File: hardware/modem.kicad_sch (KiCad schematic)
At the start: 30 parts, among them J11 PRPC001DAAN-RC, Q3 IRLML2246TRPBF, Q4 MMBT3904, U6 SN74AVC4T245PW, U7 SARA-R500S-61B

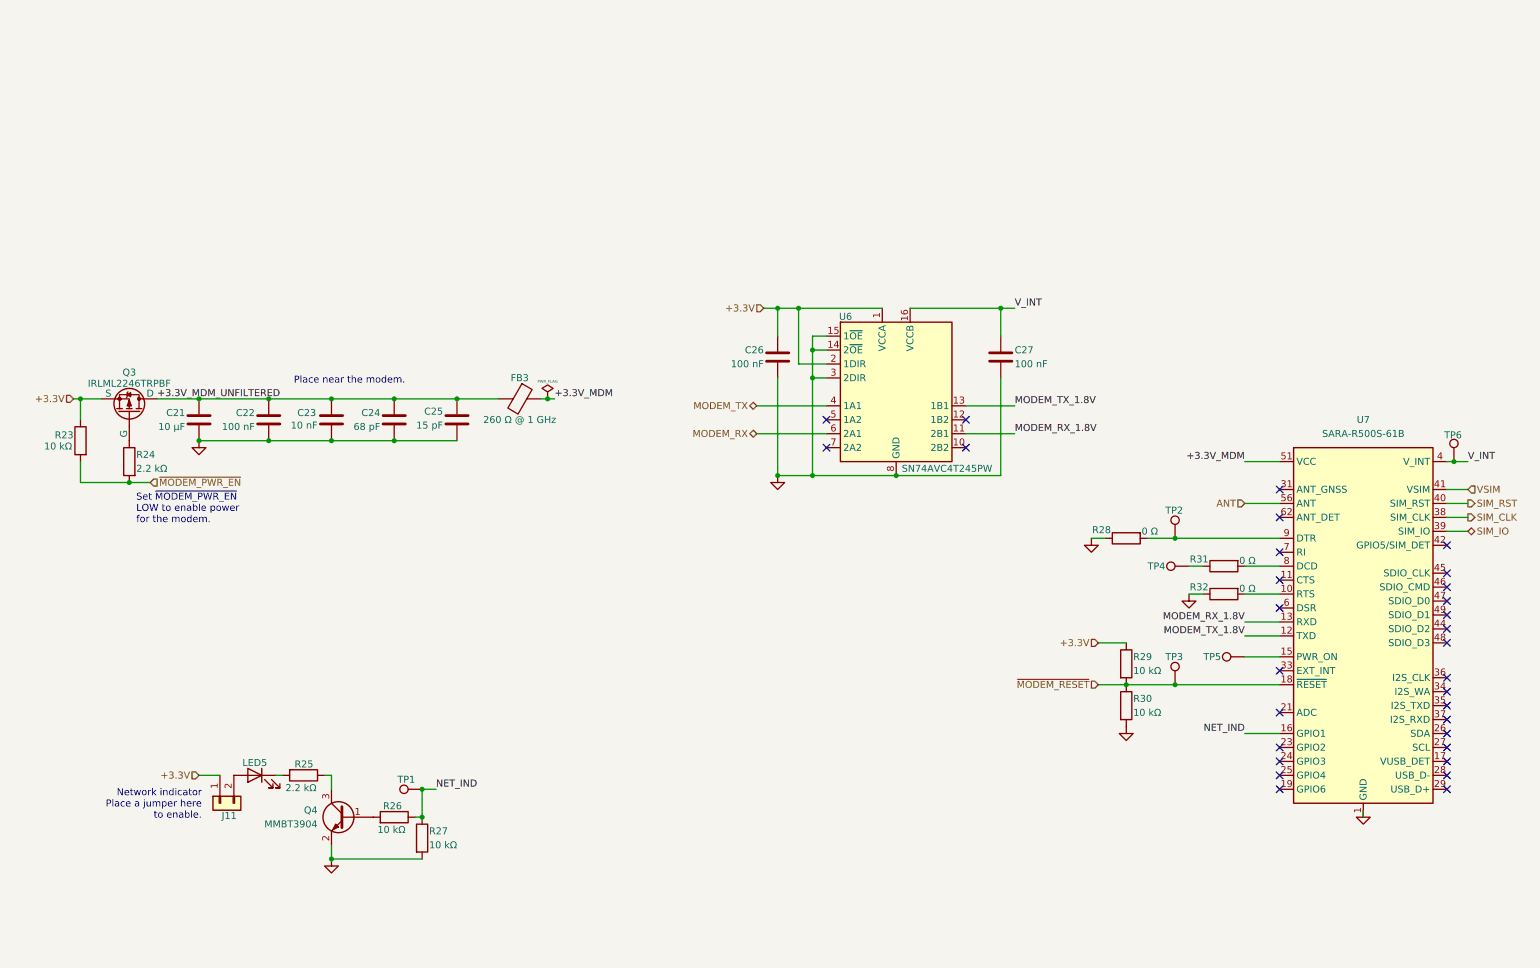
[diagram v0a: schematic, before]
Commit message: HW: Start adding Li-Po support
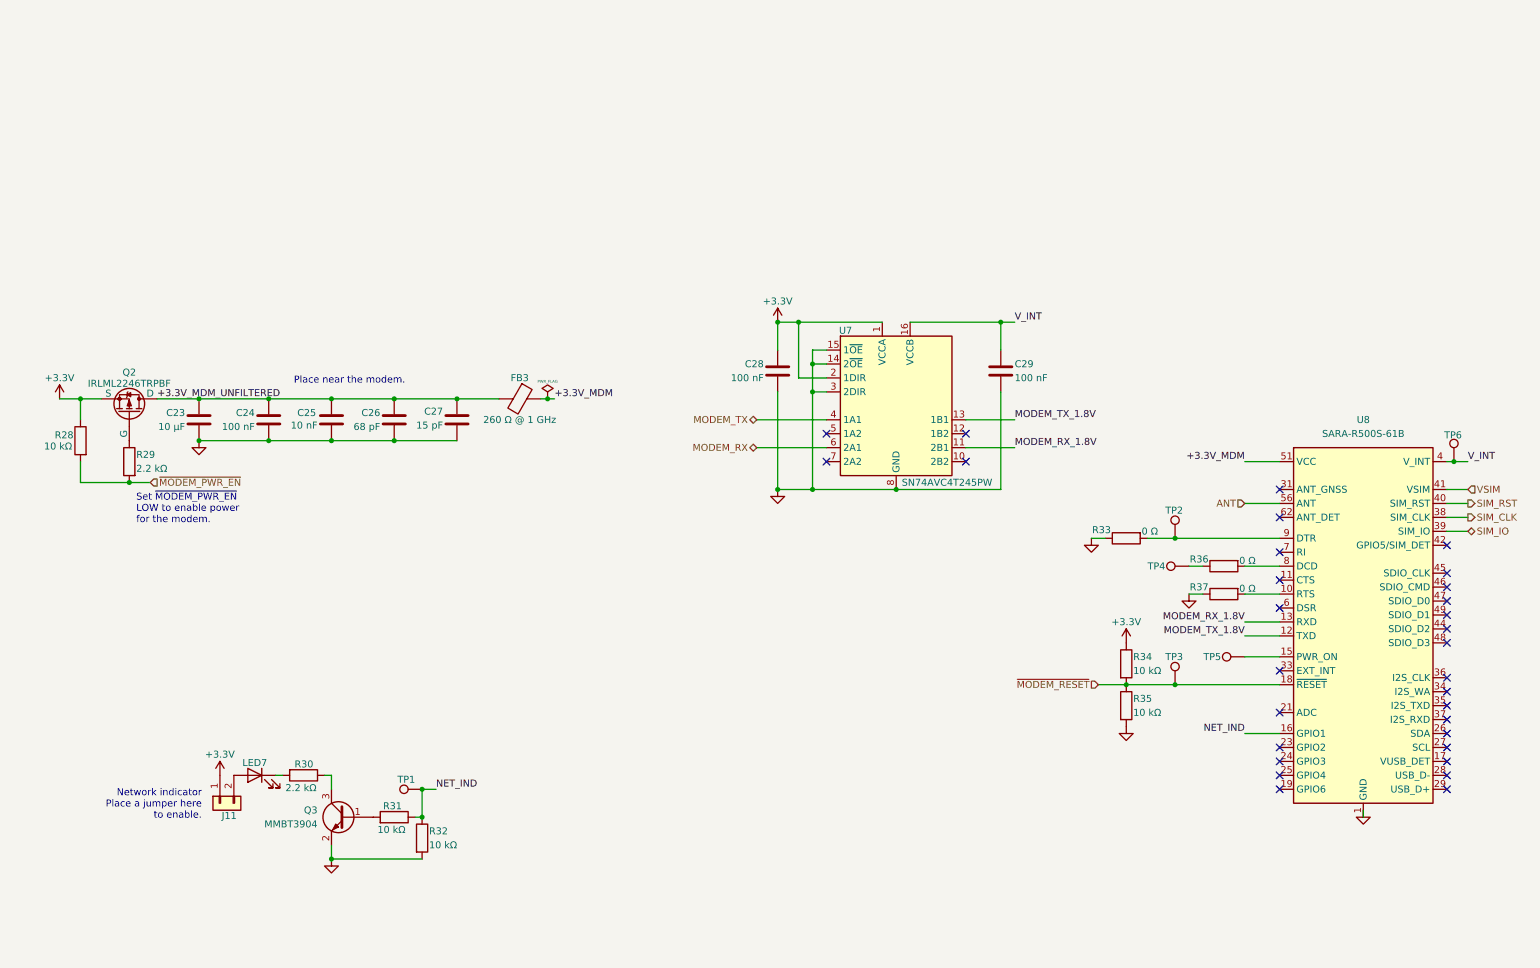
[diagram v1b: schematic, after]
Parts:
- renumbered C21 to C23, C22 to C24, C23 to C25, C24 to C26, C25 to C27, C26 to C28, C27 to C29, LED5 to LED7, Q3 to Q2, Q4 to Q3, R23 to R28, R24 to R29, R25 to R30, R26 to R31, R27 to R32, R28 to R33, R29 to R34, R30 to R35, R31 to R36, R32 to R37, U6 to U7, U7 to U8
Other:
- moved on the sheet: C28, C29, U7

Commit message: HW: Replace STM QFN with QFP
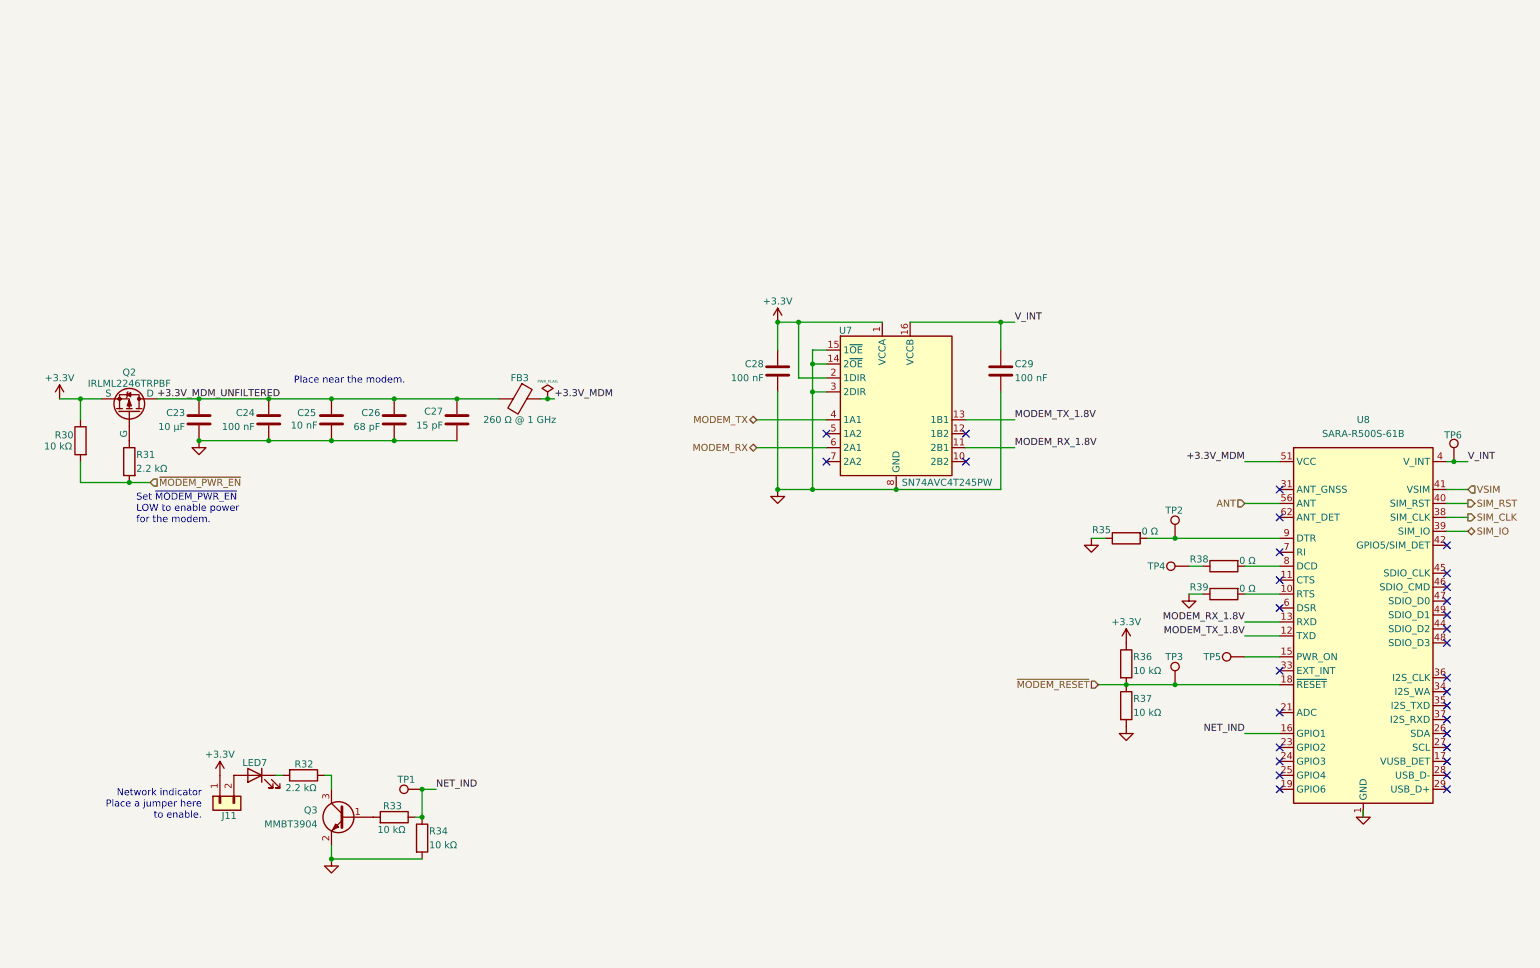
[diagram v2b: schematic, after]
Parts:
- renumbered R28 to R30, R29 to R31, R30 to R32, R31 to R33, R32 to R34, R33 to R35, R34 to R36, R35 to R37, R36 to R38, R37 to R39
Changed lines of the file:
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@@
 		(on_board yes)
 		(dnp no)
-		(property "Reference" "R34"
+		(property "Reference" "R36"
 			(at 213.36 134.62 0)
 			(effects
@@
 			(project "iida_devkit"
 				(path "/b12a6e25-97fb-4aba-bc96-af8db389bb9a/3723475b-e956-4027-ac40-e47346743900"
-					(reference "R34")
+					(reference "R36")
 					(unit 1)
 				)
@@
 		(on_board yes)
 		(dnp no)
-		(property "Reference" "#PWR040"
+		(property "Reference" "#PWR043"
 			(at 46.99 160.02 0)
 			(effects
@@
 			(project "iida_devkit"
 				(path "/b12a6e25-97fb-4aba-bc96-af8db389bb9a/3723475b-e956-4027-ac40-e47346743900"
-					(reference "#PWR040")
+					(reference "#PWR043")
 					(unit 1)
 				)
@@
 		(on_board yes)
 		(dnp no)
-		(property "Reference" "R31"
+		(property "Reference" "R33"
 			(at 76.708 161.798 90)
 			(effects
@@
 			(project "iida_devkit"
 				(path "/b12a6e25-97fb-4aba-bc96-af8db389bb9a/3723475b-e956-4027-ac40-e47346743900"
-					(reference "R31")
+					(reference "R33")
 					(unit 1)
 				)
@@
 		(on_board yes)
 		(dnp no)
-		(property "Reference" "R35"
+		(property "Reference" "R37"
 			(at 213.36 142.24 0)
 			(effects
@@
 			(project "iida_devkit"
 				(path "/b12a6e25-97fb-4aba-bc96-af8db389bb9a/3723475b-e956-4027-ac40-e47346743900"
-					(reference "R35")
+					(reference "R37")
 					(unit 1)
 				)
@@
 		(on_board yes)
 		(dnp no)
-		(property "Reference" "#PWR045"
+		(property "Reference" "#PWR048"
 			(at 212.09 135.89 0)
 			(effects
@@
 			(project "iida_devkit"
 				(path "/b12a6e25-97fb-4aba-bc96-af8db389bb9a/3723475b-e956-4027-ac40-e47346743900"
-					(reference "#PWR045")
+					(reference "#PWR048")
 					(unit 1)
 				)
@@
 		(on_board yes)
 		(dnp no)
-		(property "Reference" "R32"
+		(property "Reference" "R34"
 			(at 85.09 166.37 0)
 			(effects
@@
 			(project "iida_devkit"
 				(path "/b12a6e25-97fb-4aba-bc96-af8db389bb9a/3723475b-e956-4027-ac40-e47346743900"
-					(reference "R32")
+					(reference "R34")
 					(unit 1)
 				)
@@
 		(on_board yes)
 		(dnp no)
-		(property "Reference" "R28"
+		(property "Reference" "R30"
 			(at 20.32 94.234 0)
 			(effects
@@
 			(project "iida_devkit"
 				(path "/b12a6e25-97fb-4aba-bc96-af8db389bb9a/3723475b-e956-4027-ac40-e47346743900"
-					(reference "R28")
+					(reference "R30")
 					(unit 1)
 				)
@@
 		(dnp no)
 		(fields_autoplaced yes)
-		(property "Reference" "#PWR046"
+		(property "Reference" "#PWR049"
 			(at 212.09 153.67 0)
 			(effects
@@
 			(project "iida_devkit"
 				(path "/b12a6e25-97fb-4aba-bc96-af8db389bb9a/3723475b-e956-4027-ac40-e47346743900"
-					(reference "#PWR046")
+					(reference "#PWR049")
 					(unit 1)
 				)
@@
 		(dnp no)
 		(fields_autoplaced yes)
-		(property "Reference" "#PWR044"
+		(property "Reference" "#PWR047"
 			(at 205.74 119.38 0)
 			(effects
@@
 			(project "iida_devkit"
 				(path "/b12a6e25-97fb-4aba-bc96-af8db389bb9a/3723475b-e956-4027-ac40-e47346743900"
-					(reference "#PWR044")
+					(reference "#PWR047")
 					(unit 1)
 				)
@@
 		(dnp no)
 		(fields_autoplaced yes)
-		(property "Reference" "#PWR048"
+		(property "Reference" "#PWR051"
 			(at 255.27 168.91 0)
 			(effects
@@
 			(project "iida_devkit"
 				(path "/b12a6e25-97fb-4aba-bc96-af8db389bb9a/3723475b-e956-4027-ac40-e47346743900"
-					(reference "#PWR048")
+					(reference "#PWR051")
 					(unit 1)
 				)
@@
 		(on_board yes)
 		(dnp no)
-		(property "Reference" "R29"
+		(property "Reference" "R31"
 			(at 31.75 97.79 0)
 			(effects
@@
 			(project "iida_devkit"
 				(path "/b12a6e25-97fb-4aba-bc96-af8db389bb9a/3723475b-e956-4027-ac40-e47346743900"
-					(reference "R29")
+					(reference "R31")
 					(unit 1)
 				)
@@
 		(on_board yes)
 		(dnp no)
-		(property "Reference" "#PWR038"
+		(property "Reference" "#PWR041"
 			(at 17.78 91.44 0)
 			(effects
@@
 			(project "iida_devkit"
 				(path "/b12a6e25-97fb-4aba-bc96-af8db389bb9a/3723475b-e956-4027-ac40-e47346743900"
-					(reference "#PWR038")
+					(reference "#PWR041")
 					(unit 1)
 				)
@@
 		(on_board yes)
 		(dnp no)
-		(property "Reference" "#PWR042"
+		(property "Reference" "#PWR045"
 			(at 148.59 77.47 0)
 			(effects
@@
 			(project "iida_devkit"
 				(path "/b12a6e25-97fb-4aba-bc96-af8db389bb9a/3723475b-e956-4027-ac40-e47346743900"
-					(reference "#PWR042")
+					(reference "#PWR045")
 					(unit 1)
 				)
@@
 		(on_board yes)
 		(dnp no)
-		(property "Reference" "R37"
+		(property "Reference" "R39"
 			(at 227.076 121.92 90)
 			(effects
@@
 			(project "iida_devkit"
 				(path "/b12a6e25-97fb-4aba-bc96-af8db389bb9a/3723475b-e956-4027-ac40-e47346743900"
-					(reference "R37")
+					(reference "R39")
 					(unit 1)
 				)
@@
 		(on_board yes)
 		(dnp no)
-		(property "Reference" "R30"
+		(property "Reference" "R32"
 			(at 64.008 154.178 90)
 			(effects
@@
 			(project "iida_devkit"
 				(path "/b12a6e25-97fb-4aba-bc96-af8db389bb9a/3723475b-e956-4027-ac40-e47346743900"
-					(reference "R30")
+					(reference "R32")
 					(unit 1)
 				)
@@
 		(dnp no)
 		(fields_autoplaced yes)
-		(property "Reference" "#PWR043"
+		(property "Reference" "#PWR046"
 			(at 148.59 110.49 0)
 			(effects
@@
 			(project "iida_devkit"
 				(path "/b12a6e25-97fb-4aba-bc96-af8db389bb9a/3723475b-e956-4027-ac40-e47346743900"
-					(reference "#PWR043")
+					(reference "#PWR046")
 					(unit 1)
 				)
@@
 		(dnp no)
 		(fields_autoplaced yes)
-		(property "Reference" "#PWR039"
+		(property "Reference" "#PWR042"
 			(at 43.18 101.6 0)
 			(effects
@@
 			(project "iida_devkit"
 				(path "/b12a6e25-97fb-4aba-bc96-af8db389bb9a/3723475b-e956-4027-ac40-e47346743900"
-					(reference "#PWR039")
+					(reference "#PWR042")
 					(unit 1)
 				)
@@
 		(on_board yes)
 		(dnp no)
-		(property "Reference" "R33"
+		(property "Reference" "R35"
 			(at 209.296 111.506 90)
 			(effects
@@
 			(project "iida_devkit"
 				(path "/b12a6e25-97fb-4aba-bc96-af8db389bb9a/3723475b-e956-4027-ac40-e47346743900"
-					(reference "R33")
+					(reference "R35")
 					(unit 1)
 				)
@@
 		(dnp no)
 		(fields_autoplaced yes)
-		(property "Reference" "#PWR047"
+		(property "Reference" "#PWR050"
 			(at 223.52 129.54 0)
 			(effects
@@
 			(project "iida_devkit"
 				(path "/b12a6e25-97fb-4aba-bc96-af8db389bb9a/3723475b-e956-4027-ac40-e47346743900"
-					(reference "#PWR047")
+					(reference "#PWR050")
 					(unit 1)
 				)
@@
 		(on_board yes)
 		(dnp no)
-		(property "Reference" "R36"
+		(property "Reference" "R38"
 			(at 227.076 116.84 90)
 			(effects
@@
 			(project "iida_devkit"
 				(path "/b12a6e25-97fb-4aba-bc96-af8db389bb9a/3723475b-e956-4027-ac40-e47346743900"
-					(reference "R36")
+					(reference "R38")
 					(unit 1)
 				)
@@
 		(dnp no)
 		(fields_autoplaced yes)
-		(property "Reference" "#PWR041"
+		(property "Reference" "#PWR044"
 			(at 67.31 177.8 0)
 			(effects
@@
 			(project "iida_devkit"
 				(path "/b12a6e25-97fb-4aba-bc96-af8db389bb9a/3723475b-e956-4027-ac40-e47346743900"
-					(reference "#PWR041")
+					(reference "#PWR044")
 					(unit 1)
 				)

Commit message: HW: Update components to be hand solderable
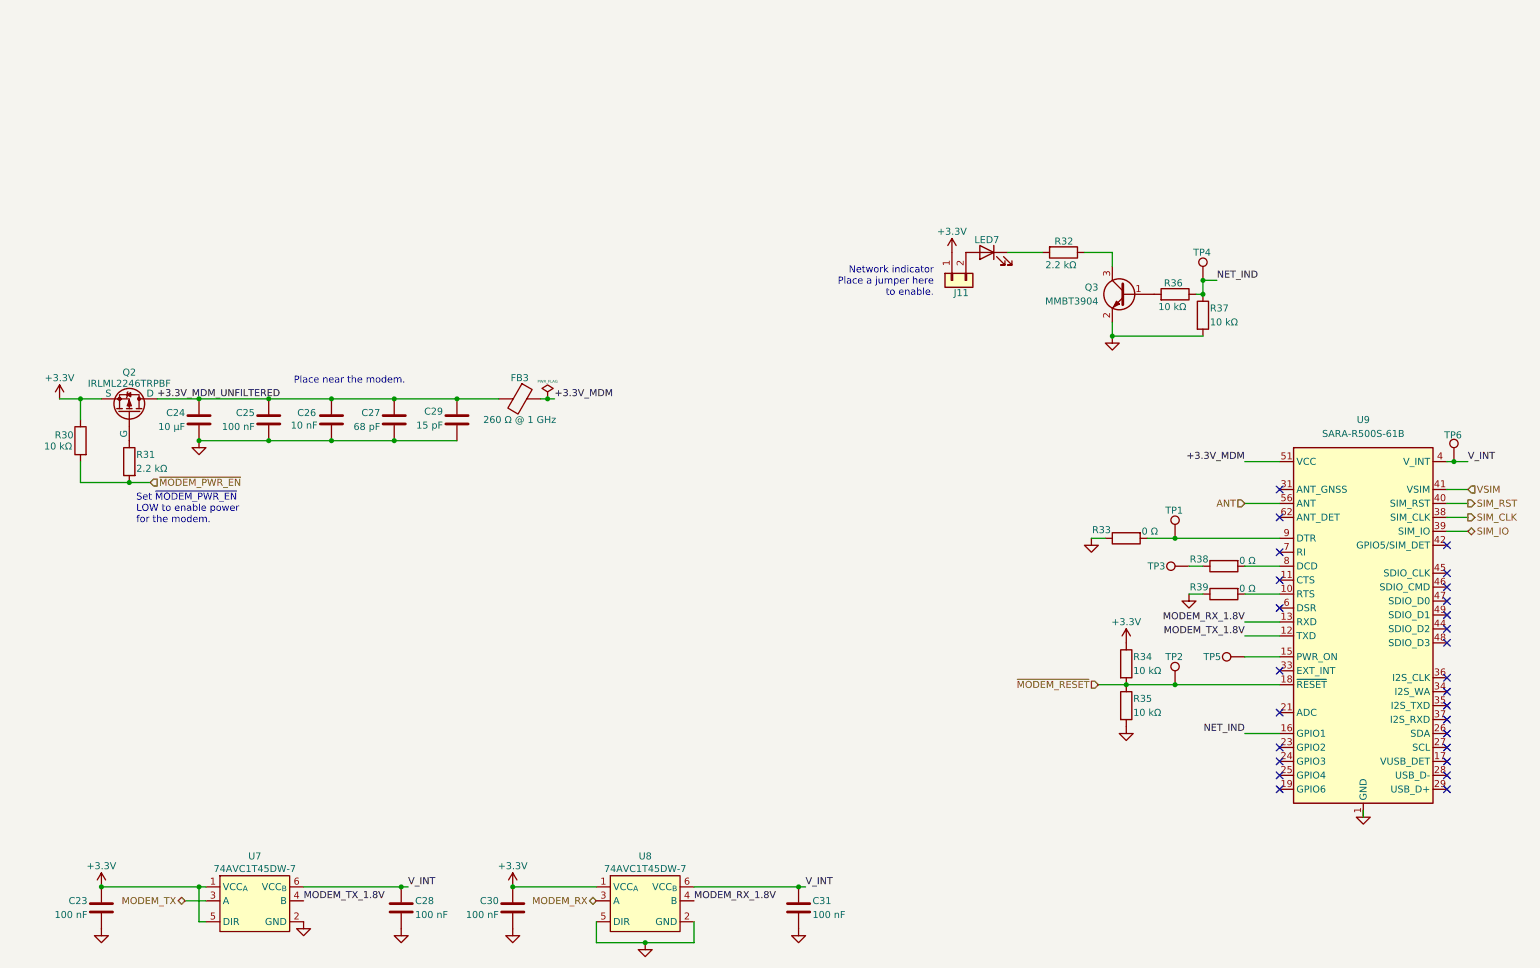
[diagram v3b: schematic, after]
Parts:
- removed C29: 100 nF, perfect_footprints:0402_1005_perfect, symbol Device:C
- removed U7: SN74AVC4T245PW, Package_SO:TSSOP-16-1EP_4.4x5mm_P0.65mm_EP3x3mm, symbol SN74AVC4T245PW:SN74AVC4T245PW
- added C23, C30, C31: 100 nF, Capacitor_SMD:C_0402_1005Metric_Pad0.74x0.62mm_HandSolder, symbol Device:C
- added U7, U8: 74AVC1T45DW-7, Package_TO_SOT_SMD:SOT-363_SC-70-6_Handsoldering, symbol 74AVC1T45DW-7:74AVC1T45DW-7
- C24: renamed from C23; footprint Capacitor_SMD:C_0603_1608Metric -> Capacitor_SMD:C_0603_1608Metric_Pad1.08x0.95mm_HandSolder
- C25: renamed from C24; footprint perfect_footprints:0402_1005_perfect -> Capacitor_SMD:C_0402_1005Metric_Pad0.74x0.62mm_HandSolder
- C26: renamed from C25; footprint perfect_footprints:0402_1005_perfect -> Capacitor_SMD:C_0402_1005Metric_Pad0.74x0.62mm_HandSolder
- C27: renamed from C26; footprint perfect_footprints:0402_1005_perfect -> Capacitor_SMD:C_0402_1005Metric_Pad0.74x0.62mm_HandSolder
- C28: footprint perfect_footprints:0402_1005_perfect -> Capacitor_SMD:C_0402_1005Metric_Pad0.74x0.62mm_HandSolder
- C29: renamed from C27; footprint perfect_footprints:0402_1005_perfect -> Capacitor_SMD:C_0402_1005Metric_Pad0.74x0.62mm_HandSolder
- FB3: footprint Resistor_SMD:R_0603_1608Metric -> Resistor_SMD:R_0603_1608Metric_Pad0.98x0.95mm_HandSolder
- LED7: footprint LED_SMD:LED_PLCC_2835 -> LED_SMD:LED_PLCC_2835_Handsoldering
- Q2: footprint Package_TO_SOT_SMD:SOT-23-3 -> Package_TO_SOT_SMD:SC-59_Handsoldering
- Q3: footprint Package_TO_SOT_SMD:SOT-23 -> Package_TO_SOT_SMD:SC-59_Handsoldering
- R30, R31, R32, R38, R39: footprint perfect_footprints:0402_1005_perfect -> Resistor_SMD:R_0402_1005Metric_Pad0.72x0.64mm_HandSolder
- R33: renamed from R35; footprint perfect_footprints:0402_1005_perfect -> Resistor_SMD:R_0402_1005Metric_Pad0.72x0.64mm_HandSolder
- R34: renamed from R36; footprint perfect_footprints:0402_1005_perfect -> Resistor_SMD:R_0402_1005Metric_Pad0.72x0.64mm_HandSolder
- R35: renamed from R37; footprint perfect_footprints:0402_1005_perfect -> Resistor_SMD:R_0402_1005Metric_Pad0.72x0.64mm_HandSolder
- R36: renamed from R33; footprint perfect_footprints:0402_1005_perfect -> Resistor_SMD:R_0402_1005Metric_Pad0.72x0.64mm_HandSolder
- R37: renamed from R34; footprint perfect_footprints:0402_1005_perfect -> Resistor_SMD:R_0402_1005Metric_Pad0.72x0.64mm_HandSolder
- renumbered TP2 to TP1, TP3 to TP2, TP4 to TP3, TP1 to TP4, U8 to U9
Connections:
- net +3.3V: now also C23.1, C30.1, U7.1 (VCC_{A}), U7.5 (DIR), U8.1 (VCC_{A}); no longer C28.1
- net GND: now also C23.2, C30.2, C31.2, U7.2 (GND), U8.2 (GND), U8.5 (DIR)
- net MODEM_RX: now also U8.3 (A)
- net MODEM_RX_1.8V: now also U8.4 (B)
- net MODEM_TX: now also U7.3 (A)
- net MODEM_TX_1.8V: now also U7.4 (B)
- net V_INT: now also C28.1, C31.1, U7.6 (VCC_{B}), U8.6 (VCC_{B})
- no-connect marks 31 -> 27
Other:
- moved on the sheet: J11, LED7, Q3, R32, R36, R37, TP4
